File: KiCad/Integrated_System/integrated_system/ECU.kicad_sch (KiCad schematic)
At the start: 50 parts, among them J1 Jack-DC, J2 Fan 1, J3 Fan 2, J4 Fan 3, Q1 BSS138, Q2 BSS138, Q3 BSS138, SW1 SW_SPDT, SW2 SW_SPDT, SW3 SW_Push, SW4 SW_Push, U1 SGP30, U2 BME680, U3 SCD30, U4 Mini360 DC to DC Buck Convert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

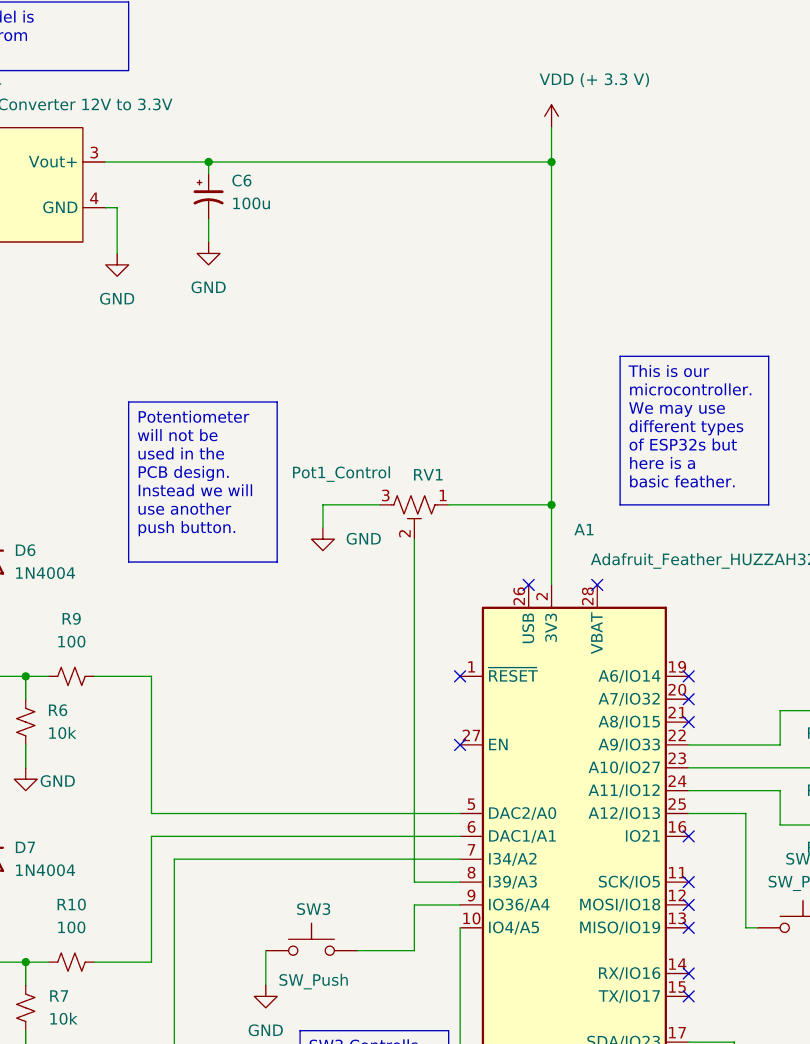
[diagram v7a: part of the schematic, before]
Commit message: deleted pot
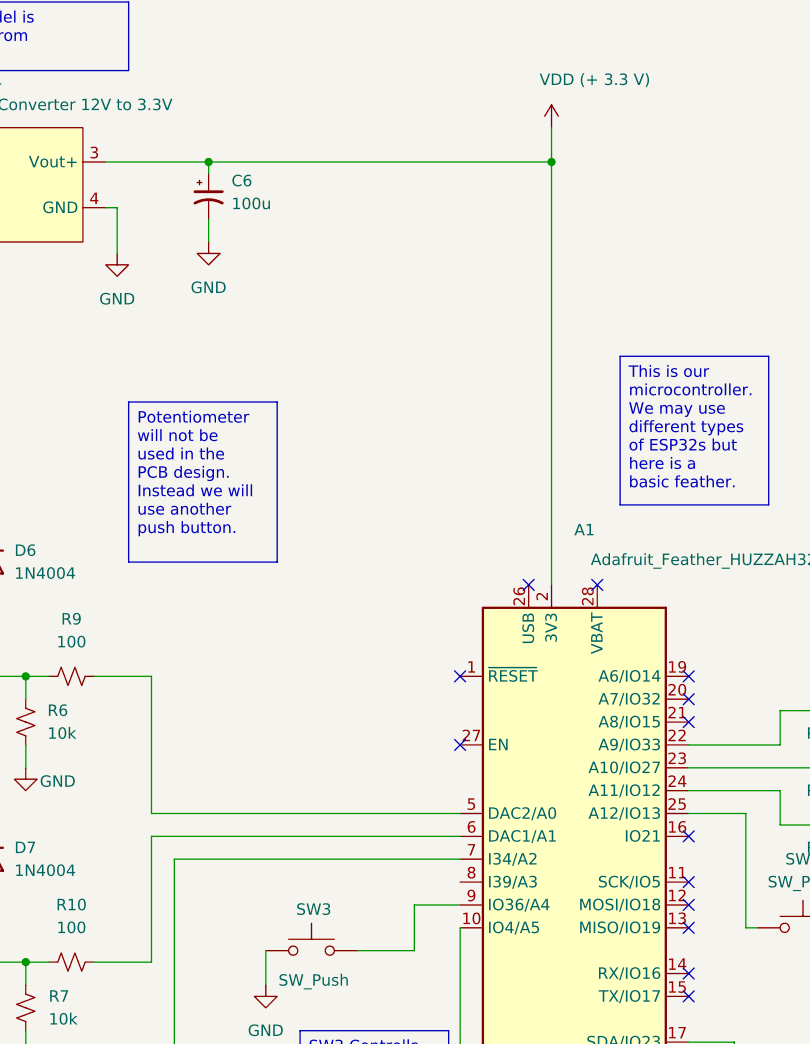
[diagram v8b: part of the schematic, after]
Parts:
- removed RV1: Pot1_Control, Potentiometer_THT:Potentiometer_Bourns_3296W_Vertical, symbol Device:R_Potentiometer_Trim_US
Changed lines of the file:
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@@
 	)
 	(junction
-		(at 205.74 69.85)
-		(diameter 0)
-		(color 0 0 0 0)
-	)
-	(junction
 		(at 223.52 146.05)
 		(diameter 0)
@@
 	(wire
 		(pts
-			(xy 194.31 69.85) (xy 205.74 69.85)
-		)
-		(stroke
-			(width 0)
-			(type default)
-		)
-	)
-	(wire
-		(pts
 			(xy 50.8 34.29) (xy 50.8 26.67)
 		)
@@
 	(wire
 		(pts
-			(xy 205.74 69.85) (xy 205.74 78.74)
+			(xy 205.74 31.75) (xy 205.74 78.74)
 		)
 		(stroke
@@
 	(wire
 		(pts
-			(xy 190.5 111.76) (xy 195.58 111.76)
-		)
-		(stroke
-			(width 0)
-			(type default)
-		)
-	)
-	(wire
-		(pts
 			(xy 157.48 36.83) (xy 157.48 41.91)
 		)
@@
 	(wire
 		(pts
-			(xy 180.34 69.85) (xy 186.69 69.85)
-		)
-		(stroke
-			(width 0)
-			(type default)
-		)
-	)
-	(wire
-		(pts
-			(xy 180.34 69.85) (xy 180.34 72.39)
-		)
-		(stroke
-			(width 0)
-			(type default)
-		)
-	)
-	(wire
-		(pts
 			(xy 135.89 138.43) (xy 135.89 140.97)
 		)
@@
 	(wire
 		(pts
-			(xy 190.5 73.66) (xy 190.5 111.76)
-		)
-		(stroke
-			(width 0)
-			(type default)
-		)
-	)
-	(wire
-		(pts
 			(xy 147.32 128.27) (xy 147.32 130.81)
 		)
@@
 	(wire
 		(pts
-			(xy 205.74 31.75) (xy 205.74 69.85)
-		)
-		(stroke
-			(width 0)
-			(type default)
-		)
-	)
-	(wire
-		(pts
 			(xy 88.9 31.75) (xy 102.87 31.75)
 		)
@@
 	)
 	(symbol
-		(lib_id "power:GND")
-		(at 180.34 72.39 0)
-		(mirror y)
-		(unit 1)
-		(exclude_from_sim no)
-		(in_bom yes)
-		(on_board yes)
-		(dnp no)
-		(fields_autoplaced yes)
-		(property "Reference" "#PWR0127"
-			(at 180.34 78.74 0)
-			(effects
-				(font
-					(size 1.27 1.27)
-				)
-				(hide yes)
-			)
-		)
-		(property "Value" "GND"
-			(at 182.88 73.6599 0)
-			(effects
-				(font
-					(size 1.27 1.27)
-				)
-				(justify right)
-			)
-		)
-		(property "Footprint" ""
-			(at 180.34 72.39 0)
-			(effects
-				(font
-					(size 1.27 1.27)
-				)
-				(hide yes)
-			)
-		)
-		(property "Datasheet" ""
-			(at 180.34 72.39 0)
-			(effects
-				(font
-					(size 1.27 1.27)
-				)
-				(hide yes)
-			)
-		)
-		(property "Description" "Power symbol creates a global label with name \"GND\" , ground"
-			(at 180.34 72.39 0)
-			(effects
-				(font
-					(size 1.27 1.27)
-				)
-				(hide yes)
-			)
-		)
-		(pin "1"
-		)
-		(instances
-			(project "ECU"
-				(path "/68e66ac2-e6c8-4149-aa8e-681ce71fac5d"
-					(reference "#PWR0127")
-					(unit 1)
-				)
-			)
-			(project "integrated_system"
-				(path "/e09e0073-4b34-4087-926d-a963f587ec36/d64a58e5-7375-438d-b343-064b897cc797"
-					(reference "#PWR020")
-					(unit 1)
-				)
-			)
-		)
-	)
-	(symbol
 		(lib_id "Device:LED")
 		(at 88.9 44.45 90)
@@
 					(unit 1)
 				)
-			)
-		)
-	)
-	(symbol
-		(lib_id "Device:R_Potentiometer_Trim_US")
-		(at 190.5 69.85 270)
-		(unit 1)
-		(exclude_from_sim no)
-		(in_bom yes)
-		(on_board yes)
-		(dnp no)
-		(property "Reference" "RV1"
-			(at 193.802 66.548 90)
-			(effects
-				(font
-					(size 1.27 1.27)
-				)
-				(justify right)
-			)
-		)
-		(property "Value" "Pot1_Control"
-			(at 187.96 66.294 90)
-			(effects
-				(font
-					(size 1.27 1.27)
-				)
-				(justify right)
-			)
-		)
-		(property "Footprint" "Potentiometer_THT:Potentiometer_Bourns_3296W_Vertical"
-			(at 190.5 69.85 0)
-			(effects
-				(font
-					(size 1.27 1.27)
-				)
-				(hide yes)
-			)
-		)
-		(property "Datasheet" "~"
-			(at 190.5 69.85 0)
-			(effects
-				(font
-					(size 1.27 1.27)
-				)
-				(hide yes)
-			)
-		)
-		(property "Description" "Trim-potentiometer, US symbol"
-			(at 190.5 69.85 0)
-			(effects
-				(font
-					(size 1.27 1.27)
-				)
-				(hide yes)
-			)
-		)
-		(pin "2"
-		)
-		(pin "3"
-		)
-		(pin "1"
-		)
-		(instances
-			(project "ECU"
-				(path "/68e66ac2-e6c8-4149-aa8e-681ce71fac5d"
-					(reference "RV1")
-					(unit 1)
-				)
-			)
-			(project "integrated_system"
-				(path "/e09e0073-4b34-4087-926d-a963f587ec36/d64a58e5-7375-438d-b343-064b897cc797"
-					(reference "RV1")
-					(unit 1)
-				)
